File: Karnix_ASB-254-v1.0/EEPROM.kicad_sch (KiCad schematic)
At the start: 3 parts, among them U6 AT24C01C-SSHM

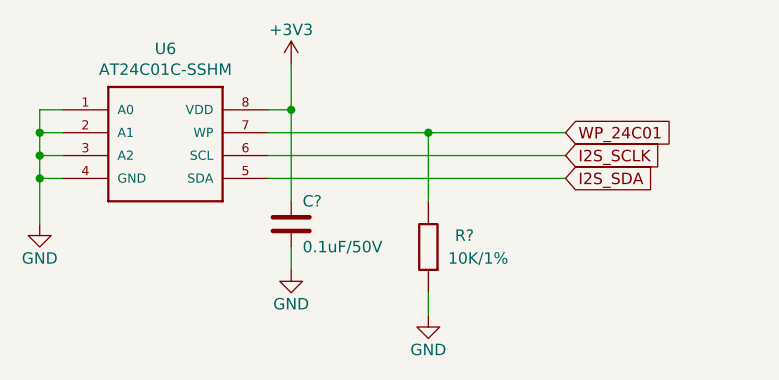
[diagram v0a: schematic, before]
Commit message: Fix EEPROM signal naming, move them to different location on FPGA
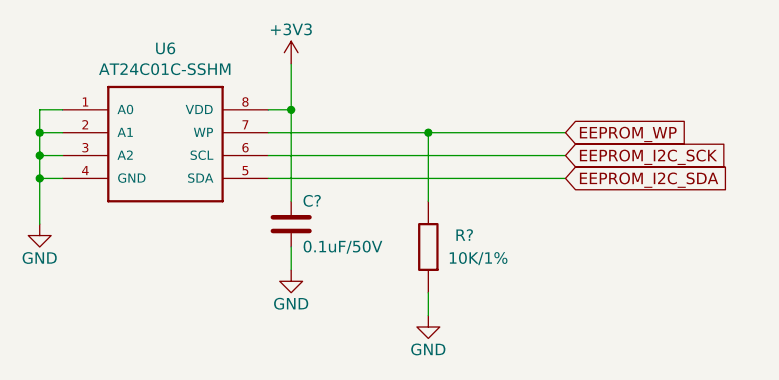
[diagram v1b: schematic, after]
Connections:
- net I2S_SCLK renamed EEPROM_I2C_SCK
- net I2S_SDA renamed EEPROM_I2C_SDA
- net WP_24C01 renamed EEPROM_WP
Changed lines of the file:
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@@
     (stroke (width 0) (type default))
   )
-  (global_label "I2S_SCLK" (shape input) (at 236.347 126.238 0)
+  (global_label "EEPROM_I2C_SCK" (shape input) (at 236.347 126.238 0)
     (effects (font (size 1.27 1.27)) (justify left))
     (property "Intersheetrefs" "${INTERSHEET_REFS}" (at 236.347 126.238 0)
@@
     )
   )
-  (global_label "WP_24C01" (shape input) (at 236.347 123.698 0)
+  (global_label "EEPROM_WP" (shape input) (at 236.347 123.698 0)
     (effects (font (size 1.27 1.27)) (justify left))
     (property "Intersheetrefs" "${INTERSHEET_REFS}" (at 236.347 123.698 0)
@@
     )
   )
-  (global_label "I2S_SDA" (shape input) (at 236.347 128.778 0)
+  (global_label "EEPROM_I2C_SDA" (shape input) (at 236.347 128.778 0)
     (effects (font (size 1.27 1.27)) (justify left))
     (property "Intersheetrefs" "${INTERSHEET_REFS}" (at 236.347 128.778 0)
